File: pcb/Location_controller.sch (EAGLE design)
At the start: 45 parts, among them IC1 LIS302DL

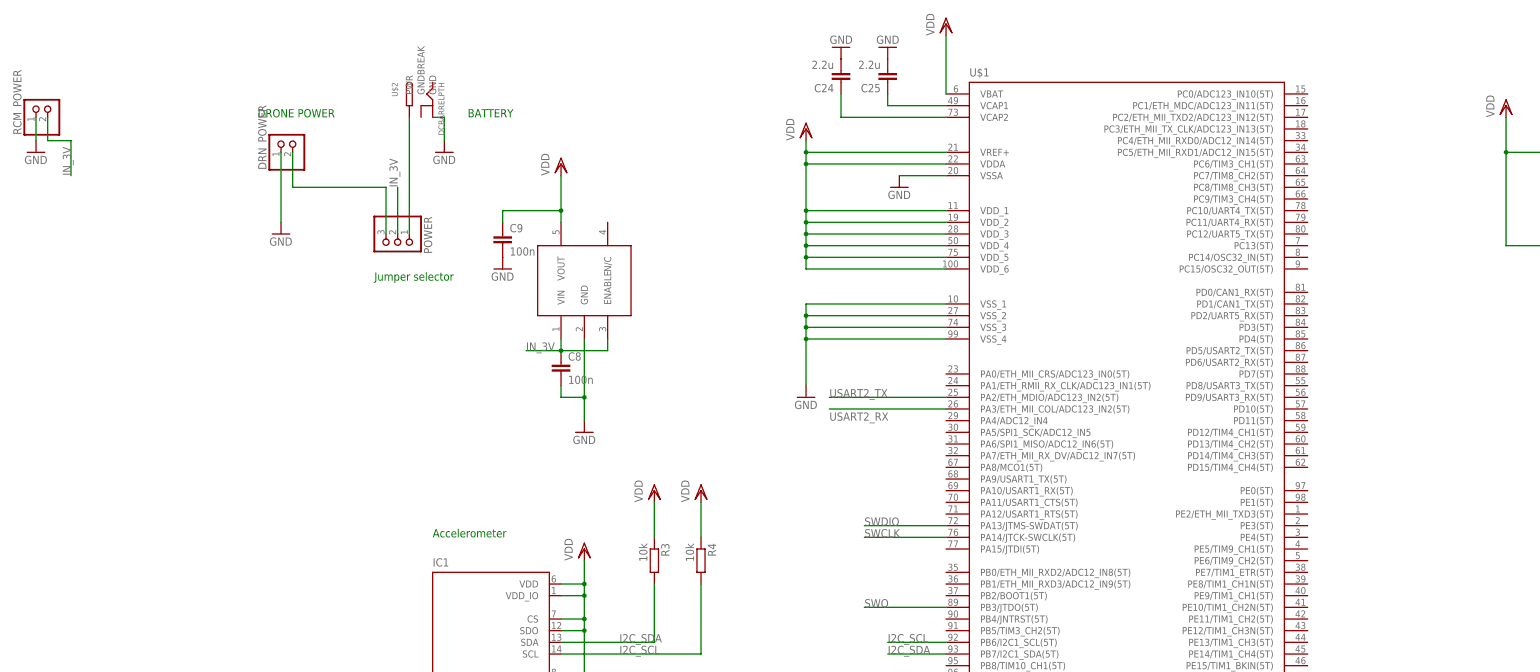
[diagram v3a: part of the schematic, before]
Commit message: Add PWR and ERR indicator LEDs
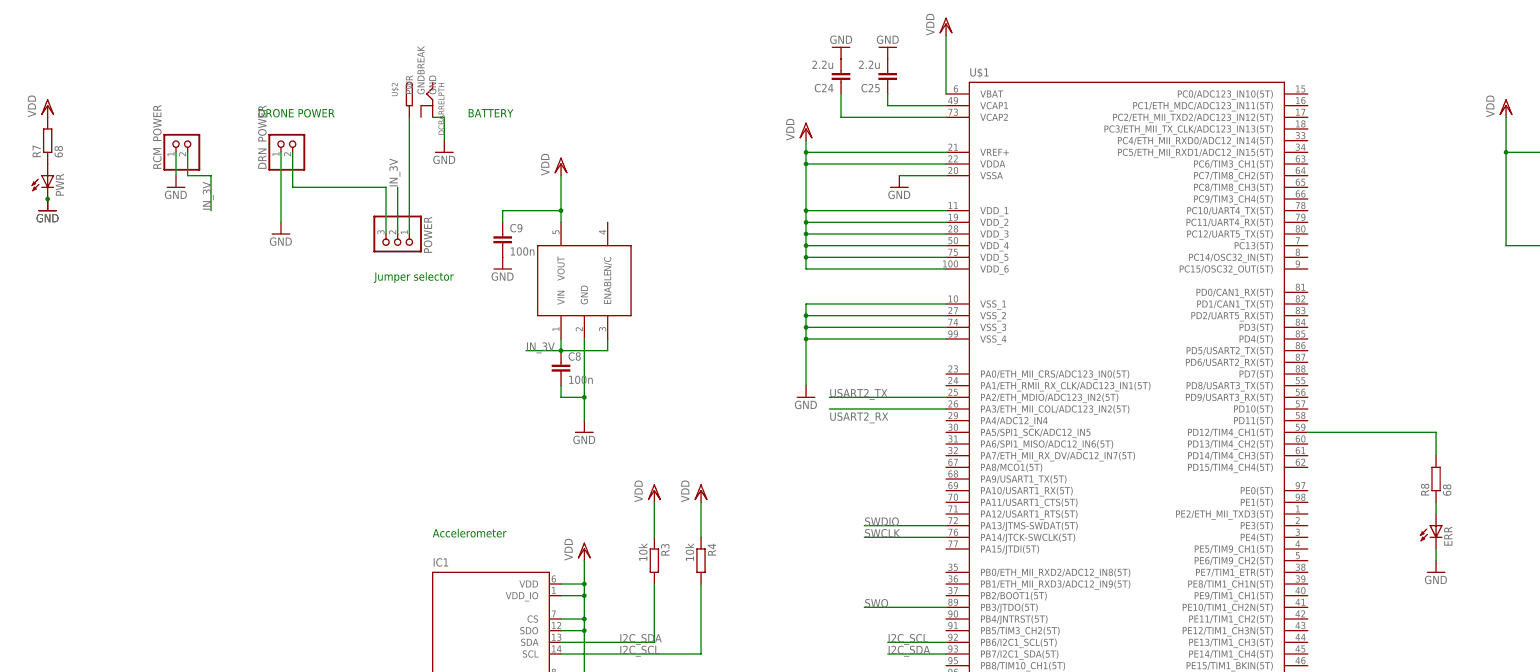
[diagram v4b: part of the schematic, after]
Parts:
- added ERR, PWR: (no value), eagle-ltspice:LED_E
- added R7, R8: 68, eagle-ltspice:R
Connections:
- new net N$12: PWR.A, R7.1
- new net N$13: ERR.A, R8.1
- new net N$14: R8.2, U$1.PD12/TIM4_CH1(5T)
- net GND: now also ERR.C, PWR.C
- net VDD: now also R7.2
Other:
- moved on the sheet: RCM_POWER
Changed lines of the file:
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@@
 <grid distance="0.1" unitdist="inch" unit="inch" style="lines" multiple="1" display="no" altdistance="0.01" altunitdist="inch" altunit="inch"/>
 <layers>
-<layer number="1" name="Top" color="4" fill="1" visible="yes" active="no"/>
-<layer number="16" name="Bottom" color="1" fill="1" visible="yes" active="no"/>
-<layer number="17" name="Pads" color="2" fill="1" visible="yes" active="no"/>
-<layer number="18" name="Vias" color="2" fill="1" visible="yes" active="no"/>
-<layer number="19" name="Unrouted" color="6" fill="1" visible="yes" active="no"/>
-<layer number="20" name="Dimension" color="15" fill="1" visible="yes" active="no"/>
-<layer number="21" name="tPlace" color="7" fill="1" visible="yes" active="no"/>
-<layer number="22" name="bPlace" color="7" fill="1" visible="yes" active="no"/>
-<layer number="23" name="tOrigins" color="15" fill="1" visible="yes" active="no"/>
-<layer number="24" name="bOrigins" color="15" fill="1" visible="yes" active="no"/>
-<layer number="25" name="tNames" color="7" fill="1" visible="yes" active="no"/>
-<layer number="26" name="bNames" color="7" fill="1" visible="yes" active="no"/>
-<layer number="27" name="tValues" color="7" fill="1" visible="yes" active="no"/>
-<layer number="28" name="bValues" color="7" fill="1" visible="yes" active="no"/>
+<layer number="1" name="Top" color="4" fill="1" visible="no" active="no"/>
+<layer number="16" name="Bottom" color="1" fill="1" visible="no" active="no"/>
+<layer number="17" name="Pads" color="2" fill="1" visible="no" active="no"/>
+<layer number="18" name="Vias" color="2" fill="1" visible="no" active="no"/>
+<layer number="19" name="Unrouted" color="6" fill="1" visible="no" active="no"/>
+<layer number="20" name="Dimension" color="15" fill="1" visible="no" active="no"/>
+<layer number="21" name="tPlace" color="7" fill="1" visible="no" active="no"/>
+<layer number="22" name="bPlace" color="7" fill="1" visible="no" active="no"/>
+<layer number="23" name="tOrigins" color="15" fill="1" visible="no" active="no"/>
+<layer number="24" name="bOrigins" color="15" fill="1" visible="no" active="no"/>
+<layer number="25" name="tNames" color="7" fill="1" visible="no" active="no"/>
+<layer number="26" name="bNames" color="7" fill="1" visible="no" active="no"/>
+<layer number="27" name="tValues" color="7" fill="1" visible="no" active="no"/>
+<layer number="28" name="bValues" color="7" fill="1" visible="no" active="no"/>
 <layer number="29" name="tStop" color="7" fill="3" visible="no" active="no"/>
 <layer number="30" name="bStop" color="7" fill="6" visible="no" active="no"/>
@@
 <layer number="35" name="tGlue" color="7" fill="4" visible="no" active="no"/>
 <layer number="36" name="bGlue" color="7" fill="5" visible="no" active="no"/>
-<layer number="37" name="tTest" color="7" fill="1" visible="yes" active="no"/>
-<layer number="38" name="bTest" color="7" fill="1" visible="yes" active="no"/>
+<layer number="37" name="tTest" color="7" fill="1" visible="no" active="no"/>
+<layer number="38" name="bTest" color="7" fill="1" visible="no" active="no"/>
 <layer number="39" name="tKeepout" color="4" fill="11" visible="no" active="no"/>
 <layer number="40" name="bKeepout" color="1" fill="11" visible="no" active="no"/>
@@
 <layer number="44" name="Drills" color="7" fill="1" visible="no" active="no"/>
 <layer number="45" name="Holes" color="7" fill="1" visible="no" active="no"/>
-<layer number="46" name="Milling" color="3" fill="1" visible="yes" active="no"/>
-<layer number="47" name="Measures" color="7" fill="1" visible="yes" active="no"/>
-<layer number="48" name="Document" color="7" fill="1" visible="yes" active="no"/>
-<layer number="49" name="Reference" color="7" fill="1" visible="yes" active="no"/>
-<layer number="50" name="dxf" color="7" fill="1" visible="yes" active="no"/>
-<layer number="51" name="tDocu" color="7" fill="1" visible="yes" active="no"/>
-<layer number="52" name="bDocu" color="7" fill="1" visible="yes" active="no"/>
-<layer number="53" name="tGND_GNDA" color="7" fill="9" visible="yes" active="no"/>
-<layer number="54" name="bGND_GNDA" color="1" fill="9" visible="yes" active="no"/>
-<layer number="56" name="wert" color="7" fill="1" visible="yes" active="no"/>
-<layer number="57" name="tCAD" color="10" fill="1" visible="yes" active="no"/>
-<layer number="58" name="bCAD" color="11" fill="1" visible="yes" active="no"/>
+<layer number="46" name="Milling" color="3" fill="1" visible="no" active="no"/>
+<layer number="47" name="Measures" color="7" fill="1" visible="no" active="no"/>
+<layer number="48" name="Document" color="7" fill="1" visible="no" active="no"/>
+<layer number="49" name="Reference" color="7" fill="1" visible="no" active="no"/>
+<layer number="50" name="dxf" color="7" fill="1" visible="no" active="no"/>
+<layer number="51" name="tDocu" color="7" fill="1" visible="no" active="no"/>
+<layer number="52" name="bDocu" color="7" fill="1" visible="no" active="no"/>
+<layer number="53" name="tGND_GNDA" color="7" fill="9" visible="no" active="no"/>
+<layer number="54" name="bGND_GNDA" color="1" fill="9" visible="no" active="no"/>
+<layer number="56" name="wert" color="7" fill="1" visible="no" active="no"/>
+<layer number="57" name="tCAD" color="10" fill="1" visible="no" active="no"/>
+<layer number="58" name="bCAD" color="11" fill="1" visible="no" active="no"/>
 <layer number="91" name="Nets" color="2" fill="1" visible="yes" active="yes"/>
 <layer number="92" name="Busses" color="1" fill="1" visible="yes" active="yes"/>
@@
 <part name="JP2" library="pinhead" deviceset="PINHD-1X6" device=""/>
 <part name="JP3" library="pinhead" deviceset="PINHD-1X6" device=""/>
+<part name="PWR" library="eagle-ltspice" deviceset="LED_E" device=""/>
+<part name="R7" library="eagle-ltspice" deviceset="R" device="" value="68"/>
+<part name="GND20" library="supply1" deviceset="GND" device=""/>
+<part name="VDD10" library="supply1" deviceset="VDD" device=""/>
+<part name="R8" library="eagle-ltspice" deviceset="R" device="" value="68"/>
+<part name="ERR" library="eagle-ltspice" deviceset="LED_E" device=""/>
+<part name="GND21" library="supply1" deviceset="GND" device=""/>
+<part name="GND22" library="supply1" deviceset="GND" device=""/>
 </parts>
 <sheets>
@@
 <instance part="DRN_POWER" gate="G$1" x="-101.6" y="121.92" rot="R90"/>
 <instance part="GND18" gate="1" x="-104.14" y="101.6"/>
-<instance part="RCM_POWER" gate="G$1" x="-154.94" y="129.54" rot="R90"/>
-<instance part="GND19" gate="1" x="-157.48" y="119.38"/>
+<instance part="RCM_POWER" gate="G$1" x="-124.46" y="121.92" rot="R90"/>
+<instance part="GND19" gate="1" x="-127" y="111.76"/>
 <instance part="U$2" gate="G$1" x="-73.66" y="132.08" rot="MR270"/>
 <instance part="JP1" gate="A" x="-33.02" y="-60.96" rot="R90"/>
 <instance part="JP2" gate="A" x="-55.88" y="-60.96" rot="R90"/>
 <instance part="JP3" gate="A" x="-78.74" y="-60.96" rot="R90"/>
+<instance part="PWR" gate="G$1" x="-154.94" y="114.3"/>
+<instance part="R7" gate="G$1" x="-154.94" y="121.92" rot="R90"/>
+<instance part="GND20" gate="1" x="-154.94" y="106.68"/>
+<instance part="VDD10" gate="G$1" x="-154.94" y="129.54"/>
+<instance part="R8" gate="G$1" x="147.32" y="48.26" rot="R90"/>
+<instance part="ERR" gate="G$1" x="147.32" y="38.1"/>
+<instance part="GND21" gate="1" x="-154.94" y="106.68"/>
+<instance part="GND22" gate="1" x="147.32" y="27.94"/>
 </instances>
 <busses>
@@
 <pinref part="RCM_POWER" gate="G$1" pin="1"/>
 <pinref part="GND19" gate="1" pin="GND"/>
-<wire x1="-157.48" y1="127" x2="-157.48" y2="121.92" width="0.1524" layer="91"/>
+<wire x1="-127" y1="119.38" x2="-127" y2="114.3" width="0.1524" layer="91"/>
 </segment>
 <segment>
@@
 <pinref part="JP1" gate="A" pin="1"/>
 <wire x1="-40.64" y1="-78.74" x2="-40.64" y2="-63.5" width="0.1524" layer="91"/>
+</segment>
+<segment>
+<pinref part="PWR" gate="G$1" pin="C"/>
+<pinref part="GND20" gate="1" pin="GND"/>
+<pinref part="GND21" gate="1" pin="GND"/>
+<junction x="-154.94" y="109.22"/>
+<pinref part="GND21" gate="1" pin="GND"/>
+</segment>
+<segment>
+<pinref part="GND22" gate="1" pin="GND"/>
+<pinref part="ERR" gate="G$1" pin="C"/>
+<wire x1="147.32" y1="30.48" x2="147.32" y2="33.02" width="0.1524" layer="91"/>
 </segment>
 </net>
@@
 <pinref part="VDD6" gate="G$1" pin="VDD"/>
 </segment>
+<segment>
+<pinref part="R7" gate="G$1" pin="2"/>
+<pinref part="VDD10" gate="G$1" pin="VDD"/>
+</segment>
 </net>
 <net name="I2C_SCL" class="0">
@@
 <segment>
 <pinref part="RCM_POWER" gate="G$1" pin="2"/>
-<wire x1="-154.94" y1="127" x2="-154.94" y2="121.92" width="0.1524" layer="91"/>
-<wire x1="-154.94" y1="121.92" x2="-149.86" y2="121.92" width="0.1524" layer="91"/>
-<wire x1="-149.86" y1="121.92" x2="-149.86" y2="114.3" width="0.1524" layer="91"/>
-<label x="-149.86" y="114.3" size="1.778" layer="95" rot="R90"/>
+<wire x1="-124.46" y1="119.38" x2="-124.46" y2="114.3" width="0.1524" layer="91"/>
+<wire x1="-124.46" y1="114.3" x2="-119.38" y2="114.3" width="0.1524" layer="91"/>
+<wire x1="-119.38" y1="114.3" x2="-119.38" y2="106.68" width="0.1524" layer="91"/>
+<label x="-119.38" y="106.68" size="1.778" layer="95" rot="R90"/>
 </segment>
 </net>
@@
 </segment>
 </net>
+<net name="N$12" class="0">
+<segment>
+<pinref part="PWR" gate="G$1" pin="A"/>
+<pinref part="R7" gate="G$1" pin="1"/>
+</segment>
+</net>
+<net name="N$13" class="0">
+<segment>
+<pinref part="ERR" gate="G$1" pin="A"/>
+<pinref part="R8" gate="G$1" pin="1"/>
+<wire x1="147.32" y1="40.64" x2="147.32" y2="43.18" width="0.1524" layer="91"/>
+</segment>
+</net>
+<net name="N$14" class="0">
+<segment>
+<pinref part="R8" gate="G$1" pin="2"/>
+<wire x1="147.32" y1="53.34" x2="147.32" y2="58.42" width="0.1524" layer="91"/>
+<pinref part="U$1" gate="G$1" pin="PD12/TIM4_CH1(5T)"/>
+<wire x1="147.32" y1="58.42" x2="119.38" y2="58.42" width="0.1524" layer="91"/>
+</segment>
+</net>

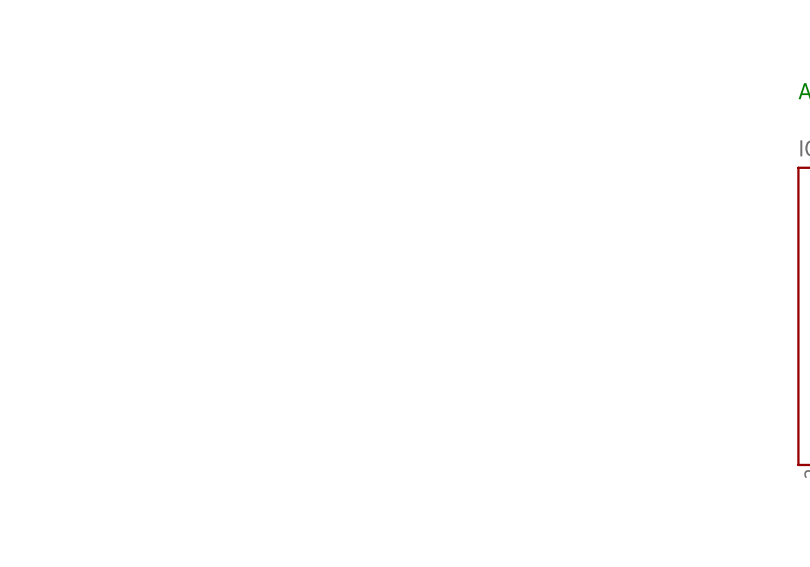
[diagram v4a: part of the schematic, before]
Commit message: Add I2C debug pins
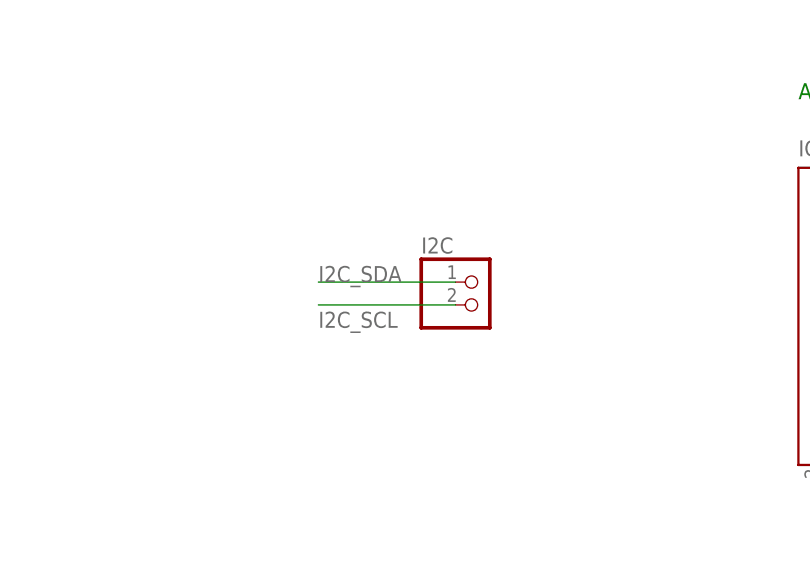
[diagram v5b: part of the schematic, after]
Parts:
- added I2C: (no value), pinhead:PINHD-1X2
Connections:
- net I2C_SCL: now also I2C.2
- net I2C_SDA: now also I2C.1
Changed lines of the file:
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@@
 <part name="GND21" library="supply1" deviceset="GND" device=""/>
 <part name="GND22" library="supply1" deviceset="GND" device=""/>
+<part name="I2C" library="pinhead" deviceset="PINHD-1X2" device=""/>
 </parts>
 <sheets>
@@
 <instance part="GND21" gate="1" x="-154.94" y="106.68"/>
 <instance part="GND22" gate="1" x="147.32" y="27.94"/>
+<instance part="I2C" gate="G$1" x="-106.68" y="12.7"/>
 </instances>
 <busses>
@@
 <wire x1="-12.7" y1="25.4" x2="-12.7" y2="10.16" width="0.1524" layer="91"/>
 </segment>
+<segment>
+<pinref part="I2C" gate="G$1" pin="2"/>
+<wire x1="-109.22" y1="12.7" x2="-124.46" y2="12.7" width="0.1524" layer="91"/>
+<label x="-124.46" y="10.16" size="1.778" layer="95"/>
+</segment>
 </net>
 <net name="I2C_SDA" class="0">
@@
 <wire x1="-22.86" y1="25.4" x2="-22.86" y2="12.7" width="0.1524" layer="91"/>
 </segment>
-</net>
+<segment>
+<pinref part="I2C" gate="G$1" pin="1"/>
+<wire x1="-109.22" y1="15.24" x2="-124.46" y2="15.24" width="0.1524" layer="91"/>
+<label x="-124.46" y="15.24" size="1.778" layer="95"/>
+</segment>
+</net>
